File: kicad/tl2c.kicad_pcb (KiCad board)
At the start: 4 copper layers, 117.5 x 66 mm, 88 parts, among them IC101 ATTINY20-X, P101 12VDC, P102 I2C Master, P103 Spare, P104 ISP Header, P105 LED_DRIVER, P106 240VAC, P107 LED_DRIVER, P108 LED_OUT, P301 PIR13, Q301 IRLML2502, Q302 IRLML2502, Q303 IRLML2502, Q401 IRLML2502, Q402 IRLML2502, Q403 IRLML2502, SW101 TL3315NF160Q, U201 LF120ABDT-TR, U202 TPS70933

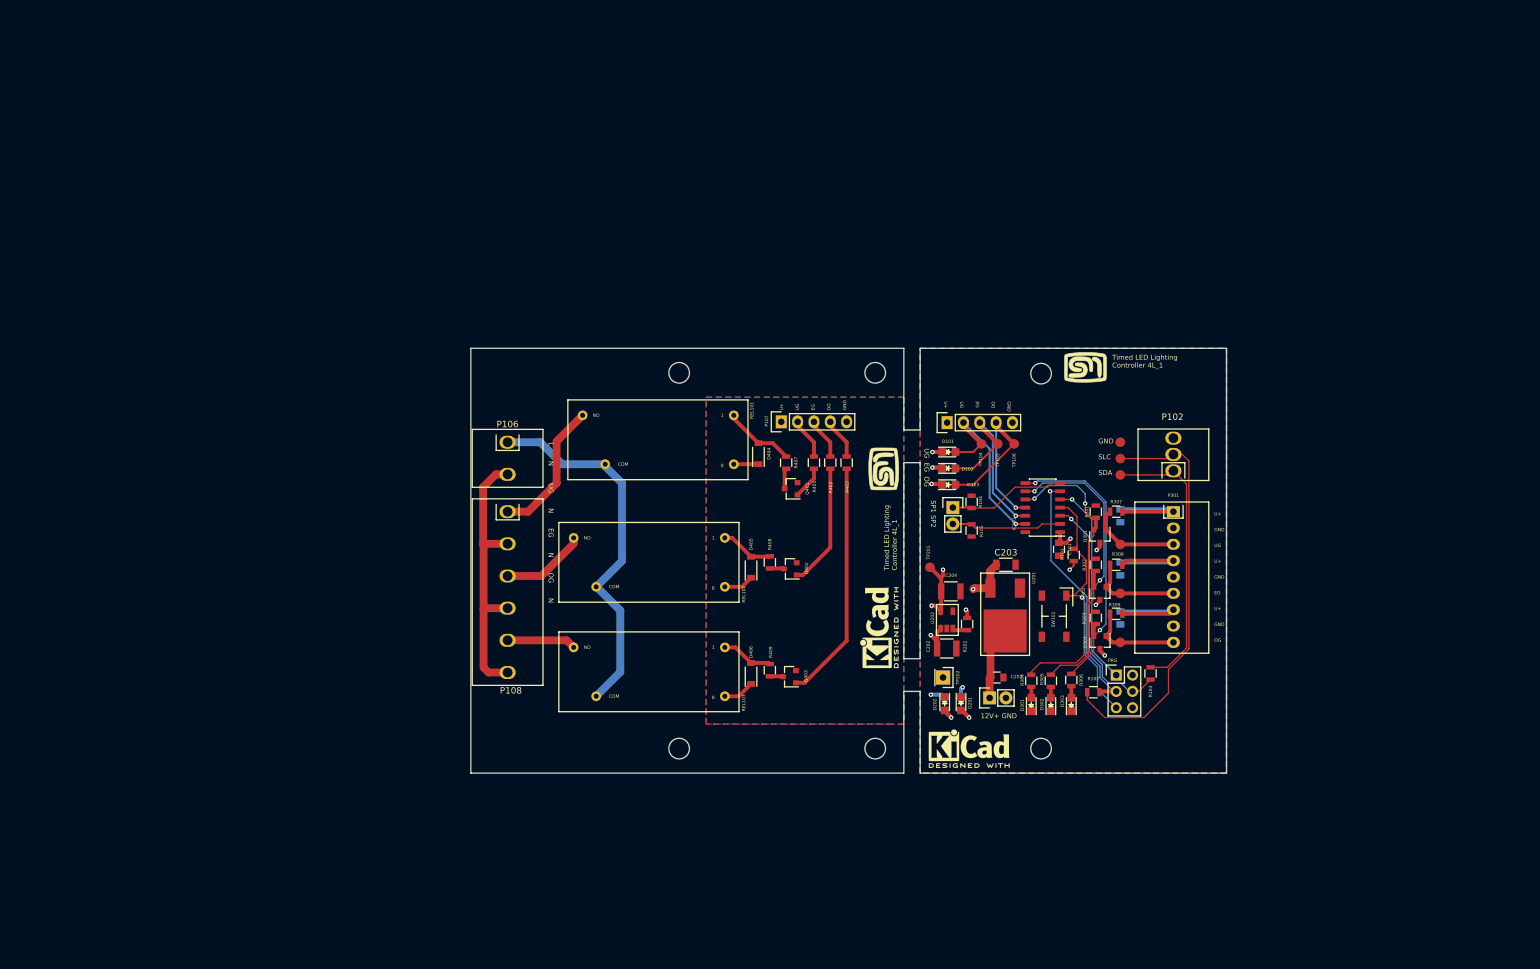
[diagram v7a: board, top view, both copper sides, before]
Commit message: The intial re-hash of the layout for the selected case
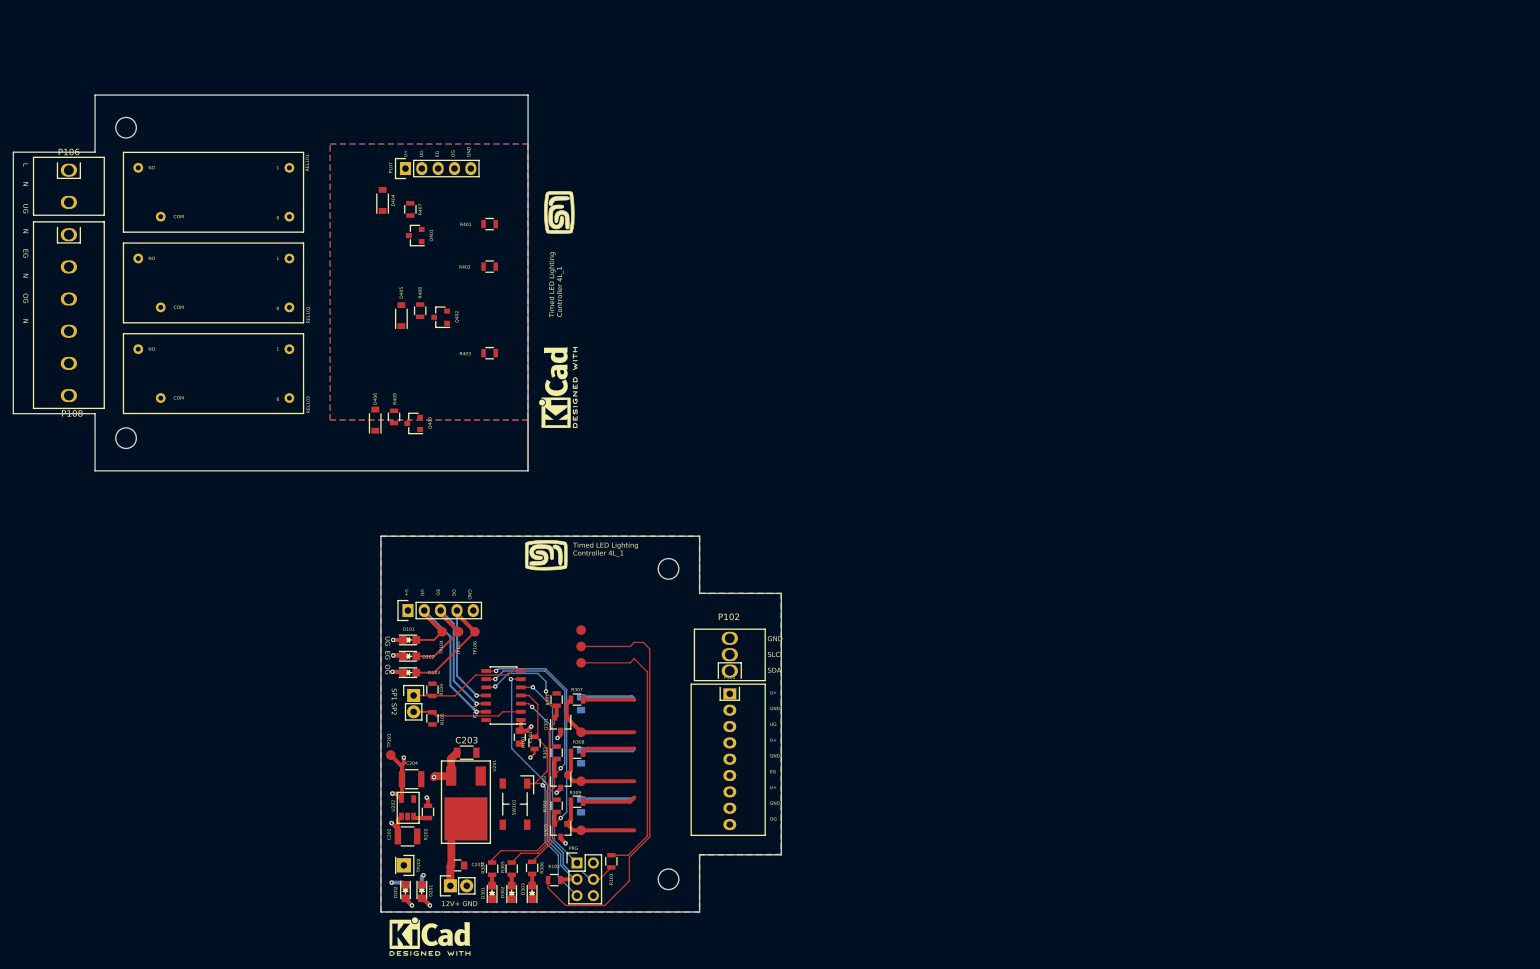
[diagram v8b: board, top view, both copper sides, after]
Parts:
- removed the REF** at (182.2, 132.1)
- removed the REF** at (182.2, 73.7)
- moved REF** 98.6 mm to (65.8, 83.8)
- moved REF** 94.0 mm to (65.8, 35.6)
- moved P104 88.8 mm to (135.9, 149.9)
- moved R103 88.8 mm to (141.2, 149.6)
- moved R307 88.8 mm to (135.9, 124.5)
- moved R308 88.8 mm to (135.9, 132.7)
- moved R309 88.8 mm to (135.9, 140.3)
- moved C201 88.8 mm to (117.3, 150.2)
- moved C204 88.8 mm to (110.2, 136.8)
- moved D101 88.8 mm to (109.9, 115.2)
- moved D102 88.8 mm to (109.9, 117.7)
- moved D103 88.8 mm to (109.9, 120.3)
- moved D201 88.8 mm to (111.8, 154.3)
- moved D301 88.8 mm to (122.7, 154.4)
- moved D302 88.8 mm to (125.7, 154.4)
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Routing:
- net /Lin: track 58.4 -> 0.00 mm
- net /Neutral: track 44.4 -> 0.00 mm
- net Net-(Q403-Pad1): track 37.3 -> 0.00 mm
- net /LineUG: track 21.7 -> 0.00 mm
- net Net-(Q402-Pad1): track 19.2 -> 0.00 mm
- net /LED Driver/LED_DRIVER_U+: track 13.7 -> 0.00 mm
- net /LineEG: track 13.2 -> 0.00 mm
- net Net-(D404-Pad2): track 11.1 -> 0.00 mm
- net /LineOG: track 10.7 -> 0.00 mm
- net Net-(D405-Pad2): track 8.24 -> 0.00 mm
- net Net-(D406-Pad2): track 8.07 -> 0.00 mm
- net /LED Driver/Relay_OG: track 6.45 -> 0.00 mm
- net /LED Driver/Relay_UG: track 6.45 -> 0.00 mm
- net /LED Driver/Relay_EG: track 6.45 -> 0.00 mm
- net Net-(Q401-Pad1): track 5.12 -> 0.00 mm
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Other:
- board size 117.5 x 66 mm -> 119.4 x 127 mm
- board text removed: "CUT OUT"
